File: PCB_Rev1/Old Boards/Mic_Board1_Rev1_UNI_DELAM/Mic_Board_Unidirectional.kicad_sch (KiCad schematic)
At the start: 31 parts, among them J2 532610771, J3 S2B-ZR-SM4A-TF_LF__SN_, U1 OPA1671IDBVR

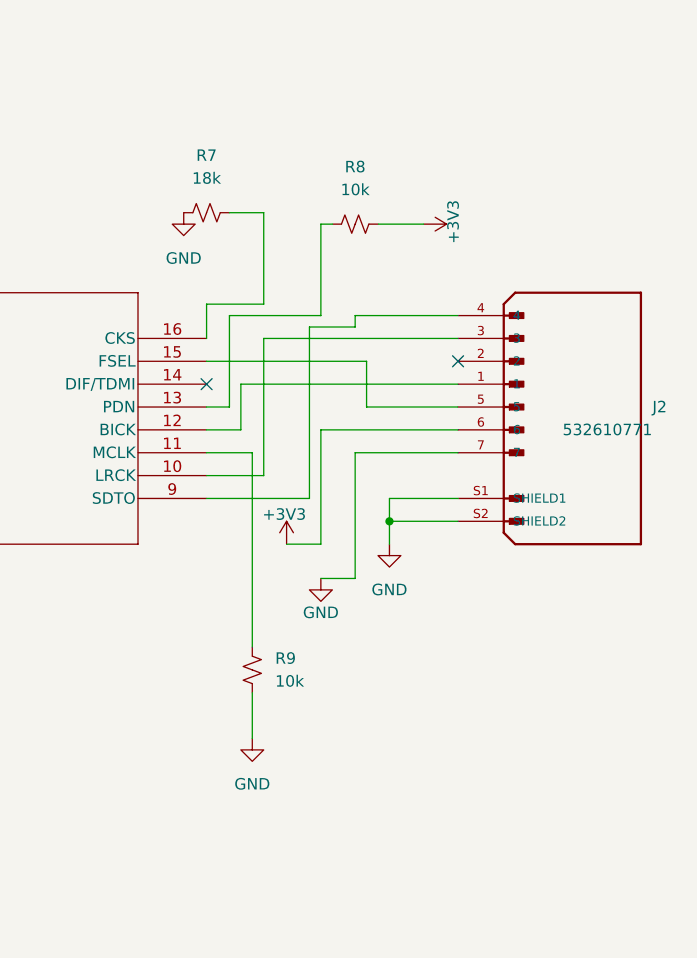
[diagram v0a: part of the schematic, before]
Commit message: new mic boards added
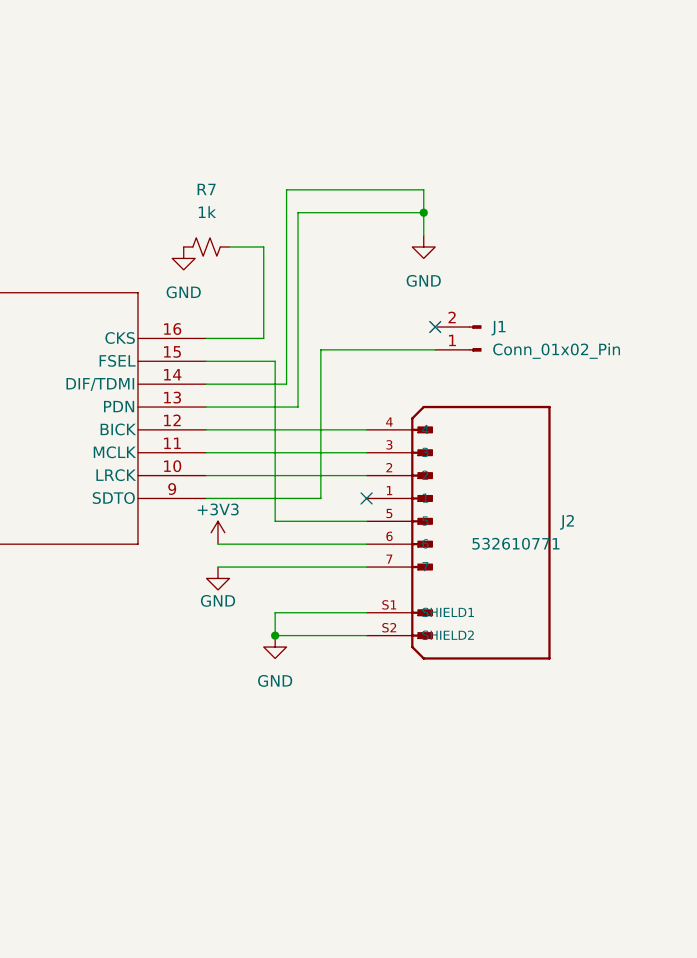
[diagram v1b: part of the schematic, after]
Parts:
- removed R8, R9: 10k, Resistor_SMD:R_0805_2012Metric, symbol Device:R_Small_US
- added J1: Conn_01x02_Pin, Connector_PinHeader_2.54mm:PinHeader_1x02_P2.54mm_Vertical, symbol Connector:Conn_01x02_Pin
- H1, H2, H3, H4: footprint MountingHole:MountingHole_3.2mm_M3 -> MountingHole:MountingHole_3.2mm_M3_DIN965_Pad
- R7: value 18k -> 1k
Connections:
- net GND: now also U2.13 (PDN), U2.14 (DIF/TDMI)
- net at U2.11 (MCLK): now also J2.3
- net at J2.1: no longer U2.12 (BICK)
- net at J2.2: now also U2.10 (LRCK)
- net at U2.9 (SDTO): now also J1.1 (Pin_1); no longer J2.4
- new net: J2.4, U2.12 (BICK)
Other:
- moved on the sheet: J2, R7
